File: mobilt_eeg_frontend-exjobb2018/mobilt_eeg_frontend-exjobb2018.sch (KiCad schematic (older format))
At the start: 120 parts, among them J1 Conn_02x04_Odd_Even, J10 Conn_01x01, J11 Conn_01x02, J12 Conn_01x01, J2 Conn_02x20_Odd_Even, J3 Conn_02x04_Odd_Even, J4 Conn_01x01, J5 Data Header, J6 Conn_01x01, J8 Conn_01x08, J9 Conn_01x04, P1 Conn_02x20_Odd_Even, SW1 SW_DIP_x01, SW2 SW_DIP_x01, U1 ADS1299-4PAG, U2 TPS60403DBVR, U3 TPS72325DBVT, U4 TPS73225DBVT, U5 TPS73233DBVT, U6 CAT24C256, X1 X1G0044810050_SG7050CAN_2.048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

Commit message: backup the weeknd
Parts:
- MK1, MK2, MK3, MK4: footprint MountingHole:MountingHole_2.7mm_M2.5 -> prj_lib_fp:MountingHole_2.7mm_M2.5
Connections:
- wire segments 498 -> 499
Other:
- note added: ">=10k pullUP"
- note added: "Double check!!"
- note removed: ">=10k pulldown"
- note removed: "PULLUP??"
- moved on the sheet: J1, R23, R24, R25, R28
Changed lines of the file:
@@
 F 0 "MK1" H -800 2296 50  0000 L CNN
 F 1 "M2.5" H -800 2205 50  0000 L CNN
-F 2 "MountingHole:MountingHole_2.7mm_M2.5" H -900 2250 60  0001 C CNN
+F 2 "prj_lib_fp:MountingHole_2.7mm_M2.5" H -900 2250 60  0001 C CNN
 F 3 "" H -900 2250 60  0001 C CNN
 	1    -900 2250
@@
 F 0 "MK3" H -350 2296 50  0000 L CNN
 F 1 "M2.5" H -350 2205 50  0000 L CNN
-F 2 "MountingHole:MountingHole_2.7mm_M2.5" H -450 2250 60  0001 C CNN
+F 2 "prj_lib_fp:MountingHole_2.7mm_M2.5" H -450 2250 60  0001 C CNN
 F 3 "" H -450 2250 60  0001 C CNN
 	1    -450 2250
@@
 F 0 "MK2" H -800 2496 50  0000 L CNN
 F 1 "M2.5" H -800 2405 50  0000 L CNN
-F 2 "MountingHole:MountingHole_2.7mm_M2.5" H -900 2450 60  0001 C CNN
+F 2 "prj_lib_fp:MountingHole_2.7mm_M2.5" H -900 2450 60  0001 C CNN
 F 3 "" H -900 2450 60  0001 C CNN
 	1    -900 2450
@@
 F 0 "MK4" H -350 2496 50  0000 L CNN
 F 1 "M2.5" H -350 2405 50  0000 L CNN
-F 2 "MountingHole:MountingHole_2.7mm_M2.5" H -450 2450 60  0001 C CNN
+F 2 "prj_lib_fp:MountingHole_2.7mm_M2.5" H -450 2450 60  0001 C CNN
 F 3 "" H -450 2450 60  0001 C CNN
 	1    -450 2450
@@
 L Connector_Generic:Conn_02x04_Odd_Even J1
 U 1 1 5B456A77
-P 16450 1400
-F 0 "J1" H 16500 975 50  0000 C CNN
-F 1 "Conn_02x04_Odd_Even" H 16500 1066 50  0000 C CNN
-F 2 "Pin_Headers:Pin_Header_Straight_2x04_Pitch2.54mm" H 16450 1400 50  0001 C CNN
-F 3 "~" H 16450 1400 50  0001 C CNN
-	1    16450 1400
+P 16500 1750
+F 0 "J1" H 16550 1325 50  0000 C CNN
+F 1 "Conn_02x04_Odd_Even" H 16550 1416 50  0000 C CNN
+F 2 "Pin_Headers:Pin_Header_Straight_2x04_Pitch2.54mm" H 16500 1750 50  0001 C CNN
+F 3 "~" H 16500 1750 50  0001 C CNN
+	1    16500 1750
 	1    0    0    1
 $EndComp
 Wire Wire Line
-	16750 1200 16750 1300
-Wire Wire Line
-	16750 1300 16750 1400
-Connection ~ 16750 1300
-Wire Wire Line
-	16750 1400 16750 1500
-Connection ~ 16750 1400
-Connection ~ 16750 1500
-$Comp
-L power:GNDD #PWR0107
-U 1 1 5B466EBF
-P 8100 1700
-F 0 "#PWR0107" H 8100 1450 50  0001 C CNN
-F 1 "GNDD" H 8104 1545 50  0000 C CNN
-F 2 "" H 8100 1700 50  0001 C CNN
-F 3 "" H 8100 1700 50  0001 C CNN
-	1    8100 1700
-	1    0    0    -1
-$EndComp
+	16800 1550 16800 1650
 NoConn ~ 10450 4400
 Text Notes 15000 900  0    50   ~ 0
@@
 Text Label 11200 2800 2    50   ~ 0
 DVDD
-Text Label 6550 1000 0    50   ~ 0
-DVDD
 Wire Notes Line
 	6500 700  8300 700
@@
 Wire Wire Line
 	8200 1000 8000 1000
-Text Label 15100 1200 0    50   ~ 0
+Text Label 15150 1550 0    50   ~ 0
 GPIO4
-Text Label 15100 1300 0    50   ~ 0
+Text Label 15150 1650 0    50   ~ 0
 GPIO3
-Text Label 15100 1400 0    50   ~ 0
+Text Label 15150 1750 0    50   ~ 0
 GPIO2
-Text Label 15100 1500 0    50   ~ 0
+Text Label 15150 1850 0    50   ~ 0
 GPIO1
 Wire Wire Line
-	15100 1500 15450 1500
-Wire Wire Line
-	15100 1200 16200 1200
-Wire Wire Line
-	15100 1400 15700 1400
-Wire Wire Line
-	15100 1300 15950 1300
-Wire Wire Line
 	10450 3000 11200 3000
 Wire Wire Line
@@
 Wire Wire Line
 	8100 1400 8100 1700
-Connection ~ 8100 1700
 Wire Wire Line
 	6900 1700 6900 1400
@@
 CLKSEL
 $Comp
-L project_symbols:DGND #PWR027
-U 1 1 5B7CDC19
-P 16750 1850
-F 0 "#PWR027" H 16750 1600 50  0001 C CNN
-F 1 "DGND" H 16754 1695 50  0000 C CNN
-F 2 "" H 16750 1850 50  0001 C CNN
-F 3 "" H 16750 1850 50  0001 C CNN
-	1    16750 1850
-	1    0    0    -1
-$EndComp
-$Comp
 L Device:R R28
 U 1 1 5B7F50C7
-P 16200 1700
-F 0 "R28" H 16270 1746 50  0000 L CNN
-F 1 "10k" H 16270 1655 50  0000 L CNN
-F 2 "Resistors_SMD:R_0805_HandSoldering" V 16130 1700 50  0001 C CNN
-F 3 "~" H 16200 1700 50  0001 C CNN
-	1    16200 1700
+P 16200 1350
+F 0 "R28" H 16270 1396 50  0000 L CNN
+F 1 "10k" H 16270 1305 50  0000 L CNN
+F 2 "Resistors_SMD:R_0805_HandSoldering" V 16130 1350 50  0001 C CNN
+F 3 "~" H 16200 1350 50  0001 C CNN
+	1    16200 1350
 	1    0    0    -1
 $EndComp
-Wire Wire Line
-	16200 1550 16200 1200
-Connection ~ 16200 1200
-Wire Wire Line
-	16200 1200 16250 1200
 $Comp
 L Device:R R25
 U 1 1 5B81CD42
-P 15950 1700
-F 0 "R25" H 16020 1746 50  0000 L CNN
-F 1 "10k" H 16020 1655 50  0000 L CNN
-F 2 "Resistors_SMD:R_0805_HandSoldering" V 15880 1700 50  0001 C CNN
-F 3 "~" H 15950 1700 50  0001 C CNN
-	1    15950 1700
+P 15950 1350
+F 0 "R25" H 16020 1396 50  0000 L CNN
+F 1 "10k" H 16020 1305 50  0000 L CNN
+F 2 "Resistors_SMD:R_0805_HandSoldering" V 15880 1350 50  0001 C CNN
+F 3 "~" H 15950 1350 50  0001 C CNN
+	1    15950 1350
 	1    0    0    -1
 $EndComp
@@
 L Device:R R24
 U 1 1 5B81CE1A
-P 15700 1700
-F 0 "R24" H 15770 1746 50  0000 L CNN
-F 1 "10k" H 15770 1655 50  0000 L CNN
-F 2 "Resistors_SMD:R_0805_HandSoldering" V 15630 1700 50  0001 C CNN
-F 3 "~" H 15700 1700 50  0001 C CNN
-	1    15700 1700
+P 15700 1350
+F 0 "R24" H 15770 1396 50  0000 L CNN
+F 1 "10k" H 15770 1305 50  0000 L CNN
+F 2 "Resistors_SMD:R_0805_HandSoldering" V 15630 1350 50  0001 C CNN
+F 3 "~" H 15700 1350 50  0001 C CNN
+	1    15700 1350
 	1    0    0    -1
 $EndComp
@@
 L Device:R R23
 U 1 1 5B81CEEA
-P 15450 1700
-F 0 "R23" H 15520 1746 50  0000 L CNN
-F 1 "10k" H 15520 1655 50  0000 L CNN
-F 2 "Resistors_SMD:R_0805_HandSoldering" V 15380 1700 50  0001 C CNN
-F 3 "~" H 15450 1700 50  0001 C CNN
-	1    15450 1700
+P 15450 1350
+F 0 "R23" H 15520 1396 50  0000 L CNN
+F 1 "10k" H 15520 1305 50  0000 L CNN
+F 2 "Resistors_SMD:R_0805_HandSoldering" V 15380 1350 50  0001 C CNN
+F 3 "~" H 15450 1350 50  0001 C CNN
+	1    15450 1350
 	1    0    0    -1
 $EndComp
-Wire Wire Line
-	15950 1550 15950 1300
-Connection ~ 15950 1300
-Wire Wire Line
-	15950 1300 16250 1300
-Wire Wire Line
-	15700 1550 15700 1400
-Connection ~ 15700 1400
-Wire Wire Line
-	15700 1400 16250 1400
-Connection ~ 15450 1500
-Wire Wire Line
-	15450 1850 15700 1850
-Connection ~ 15700 1850
-Wire Wire Line
-	15700 1850 15950 1850
-Connection ~ 15950 1850
-Wire Wire Line
-	15950 1850 16200 1850
-Wire Wire Line
-	16750 1500 16750 1850
-Wire Wire Line
-	16200 1850 16750 1850
-Connection ~ 16200 1850
-Connection ~ 16750 1850
-Wire Wire Line
-	15450 1500 16250 1500
-Wire Wire Line
-	15450 1550 15450 1500
 Wire Notes Line
 	17100 2050 15000 2050
@@
 	17100 900  17100 2050
 Text Notes 15300 2000 0    50   ~ 0
->=10k pulldown
+>=10k pullUP
 Text Notes 3850 2250 0    50   ~ 0
 Feedback Elements\n(ch.9.3.2.4.1) \nTyp. values for example only
@@
 Wire Notes Line
 	12950 4650 12950 3150
-Text Notes 15500 2200 0    50   ~ 0
-PULLUP??
 Text Label 14250 5100 0    50   ~ 0
 AVSS@1
@@
 	1    0    0    -1
 $EndComp
+Wire Wire Line
+	15150 1850 16200 1850
+Wire Wire Line
+	15150 1750 15950 1750
+Wire Wire Line
+	15150 1650 15700 1650
+Wire Wire Line
+	15150 1550 15450 1550
+$Comp
+L project_symbols:DVDD #PWR0112
+U 1 1 5B61E4B0
+P 16800 1150
+F 0 "#PWR0112" H 16800 1000 50  0001 C CNN
+F 1 "DVDD" H 16817 1323 50  0000 C CNN
+F 2 "" H 16800 1150 50  0001 C CNN
+F 3 "" H 16800 1150 50  0001 C CNN
+	1    16800 1150
+	1    0    0    -1
+$EndComp
+Connection ~ 16800 1750
+Connection ~ 16800 1650
+Wire Wire Line
+	16800 1750 16800 1850
+Wire Wire Line
+	16800 1650 16800 1750
+Wire Wire Line
+	16800 1150 16800 1200
+Connection ~ 16800 1550
+Wire Wire Line
+	16800 1200 16200 1200
+Connection ~ 16800 1200
+Wire Wire Line
+	16800 1200 16800 1550
+Connection ~ 15700 1200
+Wire Wire Line
+	15700 1200 15450 1200
+Connection ~ 15950 1200
+Wire Wire Line
+	15950 1200 15700 1200
+Connection ~ 16200 1200
+Wire Wire Line
+	16200 1200 15950 1200
+Wire Wire Line
+	15450 1500 15450 1550
+Connection ~ 15450 1550
+Wire Wire Line
+	15450 1550 16300 1550
+Wire Wire Line
+	15700 1500 15700 1650
+Connection ~ 15700 1650
+Wire Wire Line
+	15700 1650 16300 1650
+Wire Wire Line
+	15950 1500 15950 1750
+Connection ~ 15950 1750
+Wire Wire Line
+	15950 1750 16300 1750
+Wire Wire Line
+	16200 1500 16200 1850
+Connection ~ 16200 1850
+Wire Wire Line
+	16200 1850 16300 1850
+Text Notes 15350 2150 0    50   ~ 0
+Double check!!
+$Comp
+L project_symbols:DVDD #PWR0107
+U 1 1 5B8CBFDD
+P 6550 1000
+F 0 "#PWR0107" H 6550 850 50  0001 C CNN
+F 1 "DVDD" H 6567 1173 50  0000 C CNN
+F 2 "" H 6550 1000 50  0001 C CNN
+F 3 "" H 6550 1000 50  0001 C CNN
+	1    6550 1000
+	1    0    0    -1
+$EndComp
+$Comp
+L project_symbols:DGND #PWR0113
+U 1 1 5B8CC10B
+P 8100 1700
+F 0 "#PWR0113" H 8100 1450 50  0001 C CNN
+F 1 "DGND" H 8104 1545 50  0000 C CNN
+F 2 "" H 8100 1700 50  0001 C CNN
+F 3 "" H 8100 1700 50  0001 C CNN
+	1    8100 1700
+	1    0    0    -1
+$EndComp
+Connection ~ 8100 1700
 $EndSCHEMATC

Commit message: almost doonnnneeee!!!
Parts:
- removed J10: Conn_01x01, TestPoint:TestPoint_Pad_D2.0mm, symbol Connector_Generic:Conn_01x01
- removed J12, J4: Conn_01x01, Pin_Headers:Pin_Header_Straight_1x01_Pitch2.54mm, symbol Connector_Generic:Conn_01x01
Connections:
- net labels removed: GPIO12(PWM0), GPIO17(GEN0), GPIO5, GPIO7(SPI1_CE_N)
- wire segments 499 -> 498
- no-connect marks 18 -> 14
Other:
- note removed: "<-In case we need to bypass external reg."
- moved on the sheet: J5
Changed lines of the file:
@@
 Text Label 17400 1600 0    50   ~ 0
 GPIO4(GCLK)
-Text Label 17400 1800 0    50   ~ 0
-GPIO17(GEN0)
-Text Label 17400 1900 0    50   ~ 0
-GPIO27(GEN2)
 Text Label 17400 2000 0    50   ~ 0
 GPIO22(GEN3)
@@
 Text Label 17400 2600 0    50   ~ 0
 ID_SD
-Text Label 17400 2700 0    50   ~ 0
-GPIO5
 Text Label 17400 2800 0    50   ~ 0
 GPIO6
@@
 Text Label 20100 3000 2    50   ~ 0
 GPIO16
-Text Label 20100 2800 2    50   ~ 0
-GPIO12(PWM0)
 Text Label 20100 2600 2    50   ~ 0
 ID_SC
-Text Label 20100 2500 2    50   ~ 0
-GPIO7(SPI1_CE_N)
 Text Label 20100 2400 2    50   ~ 0
 GPIO8(SPI0_CE_N)
@@
 	8100 1150 8000 1150
 NoConn ~ 17400 1600
-NoConn ~ 17400 1800
 NoConn ~ 17400 1900
 NoConn ~ 17400 2000
-NoConn ~ 17400 2700
 NoConn ~ 17400 3000
 NoConn ~ 20100 1600
@@
 NoConn ~ 20100 2100
 NoConn ~ 20100 2300
-NoConn ~ 20100 2500
-NoConn ~ 20100 2800
 NoConn ~ 20100 3100
 $Comp
@@
 Wire Wire Line
 	1150 1350 1150 1150
-$Comp
-L project_symbols:ADS1299-4PAG U1
-U 1 1 5B462F68
-P 9550 3900
-F 0 "U1" H 9550 5667 50  0000 C CNN
-F 1 "ADS1299-4PAG" H 9550 5576 50  0000 C CNN
-F 2 "prj_lib_fp:xQFP_64_to_2.54mm_adapter" H 11050 5000 50  0001 L BNN
-F 3 "http://www.ti.com/lit/ds/symlink/ads1299-4.pdf" H 11000 5300 50  0001 L BNN
-F 4 "Low-Noise, 4-Channel, 24-Bit Analog-to-Digital Converter for Biopotential Measurements 64-TQFP -40 to 85" H 11000 5200 50  0001 L BNN "Description"
-F 5 "2707750" H 8947 5705 50  0001 L BNN "Farnell Part"
-F 6 "http://se.farnell.com/texas-instruments/ads1299-4pag/adc-quad-24-bits-16ksps-tqfp-64/dp/2707750" H 8847 5605 50  0001 L BNN "Farnell URL"
-	1    9550 3900
-	1    0    0    -1
-$EndComp
 Text Label 7800 4200 0    50   ~ 0
 GPIO10(SPI0_MOSI)
@@
 Wire Wire Line
 	8650 4100 9300 4100
-$Comp
-L power:GNDD #PWR0106
-U 1 1 5B65D7C1
-P 9300 4100
-F 0 "#PWR0106" H 9300 3850 50  0001 C CNN
-F 1 "GNDD" H 9304 3945 50  0000 C CNN
-F 2 "" H 9300 4100 50  0001 C CNN
-F 3 "" H 9300 4100 50  0001 C CNN
-	1    9300 4100
-	0    -1   -1   0
-$EndComp
 Text Label 13050 2650 0    50   ~ 0
 VREFP
@@
 Connection ~ 3000 8700
 Connection ~ 3000 9100
-Text Label 3450 9300 2    50   ~ 0
-SRB1
 Text Label 3450 9700 2    50   ~ 0
+SRB1
+Text Label 3450 9300 2    50   ~ 0
 SRB2
 Wire Wire Line
@@
 Text Label 3450 4450 2    50   ~ 0
 IN8P
-$Comp
-L Connector_Generic:Conn_01x01 J10
-U 1 1 5BD5918B
-P 14350 2650
-F 0 "J10" H 14430 2692 50  0000 L CNN
-F 1 "Conn_01x01" H 14430 2601 50  0000 L CNN
-F 2 "TestPoint:TestPoint_Pad_D2.0mm" H 14350 2650 50  0001 C CNN
-F 3 "~" H 14350 2650 50  0001 C CNN
-	1    14350 2650
-	1    0    0    -1
-$EndComp
 Text Notes 13500 2600 0    50   ~ 0
 Test Pad INTERNAL_VREF 4.5V
@@
 L Connector_Generic:Conn_01x10 J5
 U 1 1 5C5FECBE
-P 5550 5500
-F 0 "J5" H 5630 5492 50  0000 L CNN
-F 1 "Data Header" H 5400 4900 50  0000 L CNN
-F 2 "Pin_Headers:Pin_Header_Straight_1x10_Pitch2.54mm" H 5550 5500 50  0001 C CNN
-F 3 "~" H 5550 5500 50  0001 C CNN
-	1    5550 5500
+P 16550 3200
+F 0 "J5" H 16630 3192 50  0000 L CNN
+F 1 "Data Header" H 16400 2600 50  0000 L CNN
+F 2 "Pin_Headers:Pin_Header_Straight_1x10_Pitch2.54mm" H 16550 3200 50  0001 C CNN
+F 3 "~" H 16550 3200 50  0001 C CNN
+	1    16550 3200
 	1    0    0    -1
 $EndComp
-Text Notes 4500 4800 0    50   ~ 0
+Text Notes 15500 2500 0    50   ~ 0
 Data Header \nBetween ADS1299 & RasPi
 $Comp
 L project_symbols:DGND #PWR013
 U 1 1 5C6010BE
-P 5050 5100
-F 0 "#PWR013" H 5050 4850 50  0001 C CNN
-F 1 "DGND" H 5054 4945 50  0000 C CNN
-F 2 "" H 5050 5100 50  0001 C CNN
-F 3 "" H 5050 5100 50  0001 C CNN
-	1    5050 5100
+P 16050 2800
+F 0 "#PWR013" H 16050 2550 50  0001 C CNN
+F 1 "DGND" H 16054 2645 50  0000 C CNN
+F 2 "" H 16050 2800 50  0001 C CNN
+F 3 "" H 16050 2800 50  0001 C CNN
+	1    16050 2800
 	-1   0    0    1
 $EndComp
 Wire Wire Line
-	5050 5100 5350 5100
-$Comp
-L Connector_Generic:Conn_01x01 J12
-U 1 1 5C67C118
-P 18050 1300
-F 0 "J12" H 18130 1342 50  0000 L CNN
-F 1 "Conn_01x01" H 18130 1251 50  0000 L CNN
-F 2 "Pin_Headers:Pin_Header_Straight_1x01_Pitch2.54mm" H 18050 1300 50  0001 C CNN
-F 3 "~" H 18050 1300 50  0001 C CNN
-	1    18050 1300
-	-1   0    0    1
-$EndComp
+	16050 2800 16350 2800
 Text Notes 17350 1200 0    50   ~ 0
 In case we need to bypass extern reg.
-$Comp
-L Connector_Generic:Conn_01x01 J4
-U 1 1 5C6F47CA
-P 10900 10750
-F 0 "J4" V 11000 10700 50  0000 L CNN
-F 1 "Conn_01x01" V 10900 10850 50  0000 L CNN
-F 2 "Pin_Headers:Pin_Header_Straight_1x01_Pitch2.54mm" H 10900 10750 50  0001 C CNN
-F 3 "~" H 10900 10750 50  0001 C CNN
-	1    10900 10750
-	0    -1   -1   0
-$EndComp
-Connection ~ 10900 10950
-Text Notes 11000 10750 0    50   ~ 0
-<-In case we need to bypass external reg.
 Wire Notes Line
 	3700 3950 2450 3950
@@
 Text Notes 4400 3200 0    50   ~ 0
 Cf sets bandwidth\nof Bias Amp.
-Text Label 4600 6000 0    50   ~ 0
+Text Label 15600 3700 0    50   ~ 0
 GPIO10(SPI0_MOSI)
-Text Label 4600 5900 0    50   ~ 0
+Text Label 15600 3600 0    50   ~ 0
 ~PWDN
-Text Label 4600 5800 0    50   ~ 0
+Text Label 15600 3500 0    50   ~ 0
 ~RESET
-Text Label 4600 5700 0    50   ~ 0
+Text Label 15600 3400 0    50   ~ 0
 XTAL
-Text Label 4600 5600 0    50   ~ 0
+Text Label 15600 3300 0    50   ~ 0
 START
-Text Label 4600 5500 0    50   ~ 0
+Text Label 15600 3200 0    50   ~ 0
 GPIO8(SPI0_CE_N)
-Text Label 4600 5400 0    50   ~ 0
+Text Label 15600 3100 0    50   ~ 0
 GPIO11(SPI0_SCK)
-Text Label 4600 5300 0    50   ~ 0
+Text Label 15600 3000 0    50   ~ 0
 GPIO9(SPI0_MISO)
-Text Label 4600 5200 0    50   ~ 0
+Text Label 15600 2900 0    50   ~ 0
 ~DRDY
 Wire Wire Line
-	5350 5200 4600 5200
+	16350 2900 15600 2900
 Wire Wire Line
-	4600 5300 5350 5300
+	15600 3000 16350 3000
 Wire Wire Line
-	5350 5400 4600 5400
+	16350 3100 15600 3100
 Wire Wire Line
-	4600 5500 5350 5500
+	15600 3200 16350 3200
 Wire Wire Line
-	5350 5600 4600 5600
+	16350 3300 15600 3300
 Wire Wire Line
-	4600 5700 5350 5700
+	15600 3400 16350 3400
 Wire Wire Line
-	5350 5800 4600 5800
+	16350 3500 15600 3500
 Wire Wire Line
-	4600 5900 5350 5900
+	15600 3600 16350 3600
 Wire Wire Line
-	5350 6000 4600 6000
+	16350 3700 15600 3700
 $Comp
 L project_symbols:AGND #PWR03
@@
 	12950 7900 14600 7900
 Wire Notes Line
-	4500 4800 4500 6200
+	15500 2500 15500 3900
 Wire Notes Line
-	4500 6200 5950 6200
+	15500 3900 16950 3900
 Wire Notes Line
-	5950 6200 5950 4800
+	16950 3900 16950 2500
 Wire Notes Line
-	5950 4800 4500 4800
+	16950 2500 15500 2500
 Text Label 18850 7200 2    50   ~ 0
 GPIO26
@@
 Wire Wire Line
 	16800 1150 16800 1200
-Connection ~ 16800 1550
 Wire Wire Line
 	16800 1200 16200 1200
-Connection ~ 16800 1200
-Wire Wire Line
-	16800 1200 16800 1550
 Connection ~ 15700 1200
 Wire Wire Line
@@
 $EndComp
 Connection ~ 8100 1700
+$Comp
+L project_symbols:ADS1299-4PAG U1
+U 1 1 5B462F68
+P 9550 3900
+F 0 "U1" H 9550 5667 50  0000 C CNN
+F 1 "ADS1299-4PAG" H 9550 5576 50  0000 C CNN
+F 2 "prj_lib_fp:xQFP_64_to_2.54mm_adapter" H 11050 5000 50  0001 L BNN
+F 3 "http://www.ti.com/lit/ds/symlink/ads1299-4.pdf" H 11000 5300 50  0001 L BNN
+F 4 "Low-Noise, 4-Channel, 24-Bit Analog-to-Digital Converter for Biopotential Measurements 64-TQFP -40 to 85" H 11000 5200 50  0001 L BNN "Description"
+F 5 "2707750" H 8947 5705 50  0001 L BNN "Farnell Part"
+F 6 "http://se.farnell.com/texas-instruments/ads1299-4pag/adc-quad-24-bits-16ksps-tqfp-64/dp/2707750" H 8847 5605 50  0001 L BNN "Farnell URL"
+	1    9550 3900
+	1    0    0    -1
+$EndComp
+$Comp
+L project_symbols:DGND #PWR0106
+U 1 1 5B8D02EB
+P 9300 4100
+F 0 "#PWR0106" H 9300 3850 50  0001 C CNN
+F 1 "DGND" H 9304 3945 50  0000 C CNN
+F 2 "" H 9300 4100 50  0001 C CNN
+F 3 "" H 9300 4100 50  0001 C CNN
+	1    9300 4100
+	1    0    0    -1
+$EndComp
+$Comp
+L project_symbols:DGND #PWR0114
+U 1 1 5B8D16DF
+P 16800 1850
+F 0 "#PWR0114" H 16800 1600 50  0001 C CNN
+F 1 "DGND" H 16804 1695 50  0000 C CNN
+F 2 "" H 16800 1850 50  0001 C CNN
+F 3 "" H 16800 1850 50  0001 C CNN
+	1    16800 1850
+	1    0    0    -1
+$EndComp
+Connection ~ 16800 1850
+Text Label 17400 1900 0    50   ~ 0
+GPIO27(GEN2)
+Text Label 17400 1800 0    50   ~ 0
+~DRDY
+Text Label 20100 2500 0    50   ~ 0
+START
+Text Label 17400 2700 0    50   ~ 0
+~RESET
+Text Label 20100 2800 0    50   ~ 0
+~PWDN
 $EndSCHEMATC

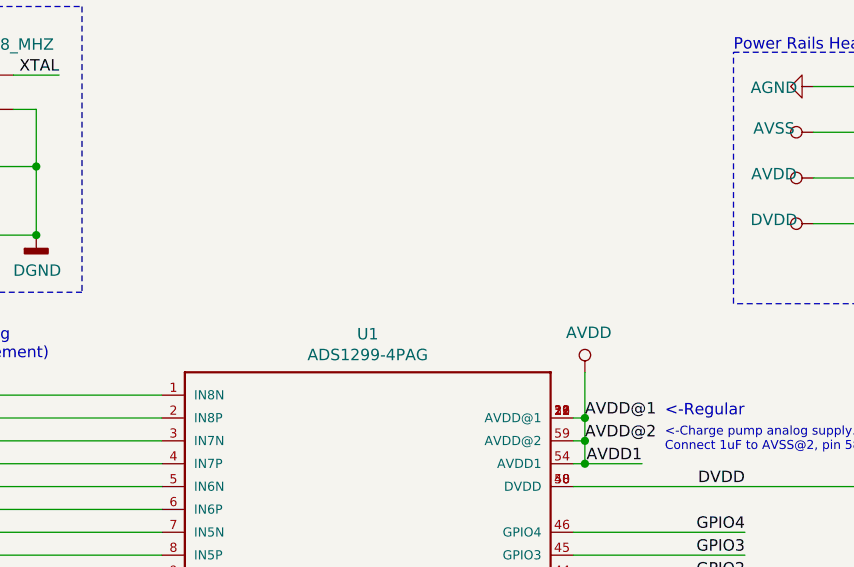
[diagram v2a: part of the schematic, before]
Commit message: labeled some headers/moved some silk covering pads
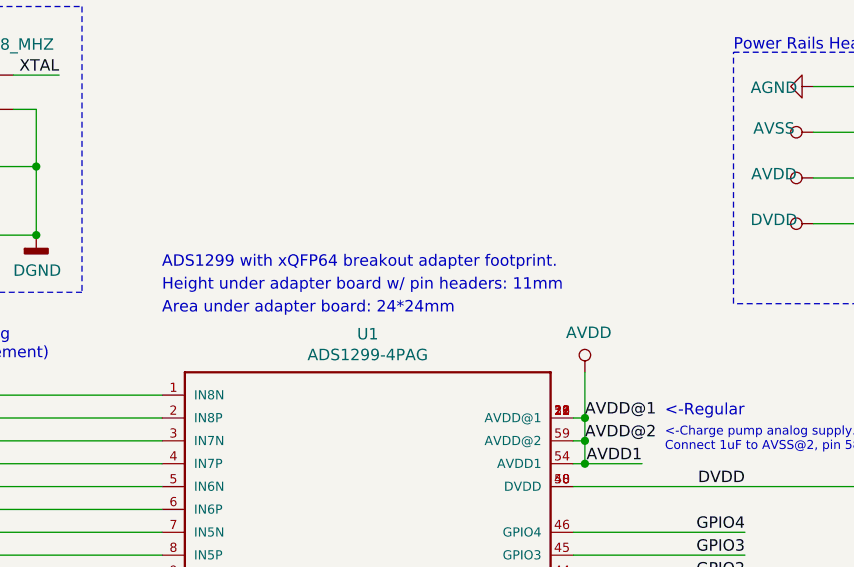
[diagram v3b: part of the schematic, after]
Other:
- note added: "ADS1299 with xQFP64 breakout adapter footprint."
- note added: "Area under adapter board: 24*24mm"
- note added: "Height under adapter board w/ pin headers: 11mm"
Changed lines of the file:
@@
 Text Label 20100 2800 0    50   ~ 0
 ~PWDN
+Text Notes 8650 1850 0    50   ~ 0
+ADS1299 with xQFP64 breakout adapter footprint.
+Text Notes 8650 1950 0    50   ~ 0
+Height under adapter board w/ pin headers: 11mm
+Text Notes 8650 2050 0    50   ~ 0
+Area under adapter board: 24*24mm
 $EndSCHEMATC

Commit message: fine tuning etc...
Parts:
- removed J6: Conn_01x01, TestPoint:TestPoint_Pad_D2.0mm, symbol Connector_Generic:Conn_01x01
- J3: footprint Pin_Headers:Pin_Header_Straight_2x04_Pitch2.54mm -> prj_lib_fp:Pin_Header_Straight_2x04_Pitch2.54mm
- J8: footprint Pin_Headers:Pin_Header_Straight_1x08_Pitch2.54mm -> prj_lib_fp:Pin_Header_Straight_1x08_Pitch2.54mm
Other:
- note added: "Implemented with a via."
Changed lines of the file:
@@
 F 0 "J8" H 11900 1750 50  0000 L CNN
 F 1 "Conn_01x08" H 11700 850 50  0000 L CNN
-F 2 "Pin_Headers:Pin_Header_Straight_1x08_Pitch2.54mm" H 11900 1350 50  0001 C CNN
+F 2 "prj_lib_fp:Pin_Header_Straight_1x08_Pitch2.54mm" H 11900 1350 50  0001 C CNN
 F 3 "~" H 11900 1350 50  0001 C CNN
 	1    11900 1350
@@
 Wire Wire Line
 	2100 9700 2800 9700
-$Comp
-L Connector_Generic:Conn_01x01 J6
-U 1 1 5BCD7365
-P 11200 6650
-F 0 "J6" H 11280 6692 50  0000 L CNN
-F 1 "Conn_01x01" H 11280 6601 50  0000 L CNN
-F 2 "TestPoint:TestPoint_Pad_D2.0mm" H 11200 6650 50  0001 C CNN
-F 3 "~" H 11200 6650 50  0001 C CNN
-	1    11200 6650
-	1    0    0    -1
-$EndComp
 Wire Wire Line
 	10150 6650 11000 6650
@@
 F 0 "J3" H 3050 2817 50  0000 C CNN
 F 1 "Conn_02x04_Odd_Even" H 3050 2726 50  0000 C CNN
-F 2 "Pin_Headers:Pin_Header_Straight_2x04_Pitch2.54mm" H 3000 2500 50  0001 C CNN
+F 2 "prj_lib_fp:Pin_Header_Straight_2x04_Pitch2.54mm" H 3000 2500 50  0001 C CNN
 F 3 "~" H 3000 2500 50  0001 C CNN
 	1    3000 2500
@@
 Text Notes 8650 2050 0    50   ~ 0
 Area under adapter board: 24*24mm
+Text Notes 11000 6600 0    50   ~ 0
+Implemented with a via.
 $EndSCHEMATC
